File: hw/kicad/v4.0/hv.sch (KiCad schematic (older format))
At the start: 21 parts, among them P13 CONN_01X04, P2 CONN_01X02, Q5 IRLML6344, U24 non_plated, U3 SI8621, U30 non_plated, U31 non_plated

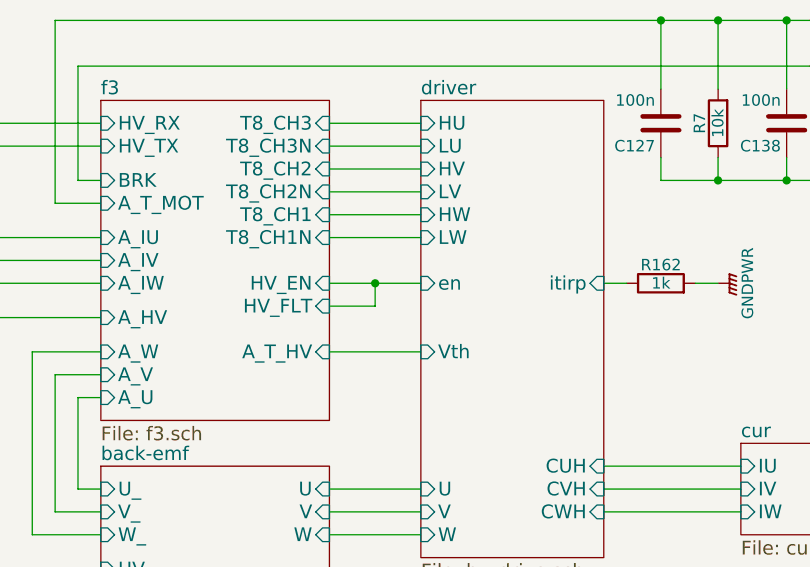
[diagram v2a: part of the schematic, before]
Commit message: changes for IKCM30F60GD
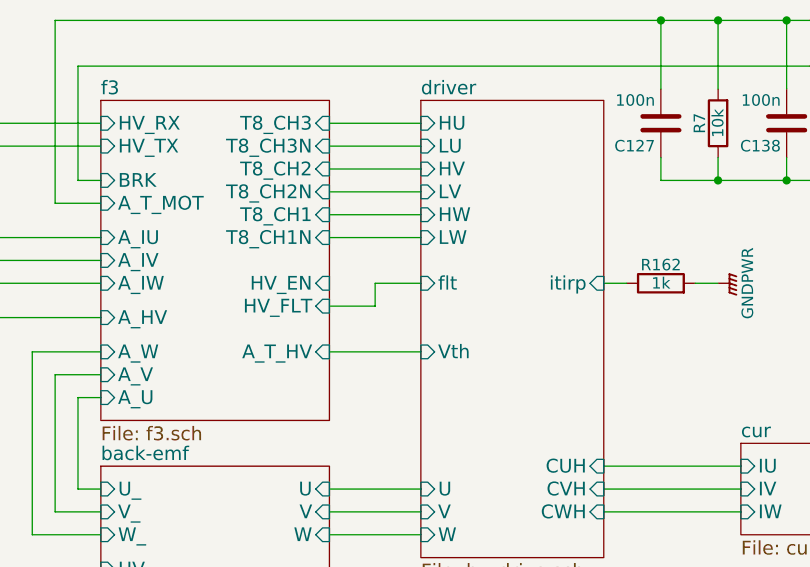
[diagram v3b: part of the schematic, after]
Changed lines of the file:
@@
 F10 "HW" I L 7400 2300 60
 F11 "LW" I L 7400 2400 60
-F12 "en" I L 7400 2600 60
+F12 "flt" I L 7400 2600 60
 F13 "itirp" I R 8200 2600 60
 F14 "CUH" I R 8200 3400 60
@@
 	7000 2400 7400 2400
 Wire Wire Line
-	7000 2600 7200 2600
-Wire Wire Line
 	7000 2700 7200 2700
 Wire Wire Line
 	7200 2700 7200 2600
-Connection ~ 7200 2600
 Wire Wire Line
 	7000 2900 7400 2900
